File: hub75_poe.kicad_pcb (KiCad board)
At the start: 4 copper layers, 70.5 x 48.3 mm, 98 parts, among them J1 0826-1X1T-JK-F, J2 Conn_02x08_Odd_Even, J3 Conn_02x04_Odd_Even, Q1 FDS2582, Q2 FDS8880, SW1 SW_SPST, T1 PA2369NL, T2 PE-68386NL, U1 KSZ8081MLX, U10 SN74LVC8T245, U11 SN74LVC8T245, U12 OSC_100M, U2 ICE40HX8K-BG121, U3 LTC4269-1, U4 TPS74633, U5 TPS74612, U6 W25Q32JVSS, U7 S27KL0641, U8 OSC_25M, U9 TPS74618

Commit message: Routing changes, pullups, etc
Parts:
- added J4: Conn_01x04, Connector_Molex:Molex_CLIK-Mate_502382-0970_1x09-1MP_P1.25mm_Vertical, B.Cu at (180.7, 69.2)
- added J5: 7466003R, hub75_poe:7466003R, F.Cu at (180.1, 95.4)
- added R25: 10k, Resistor_SMD:R_0402_1005Metric, F.Cu at (183.1, 60.8)
- added R26: 10k, Resistor_SMD:R_0402_1005Metric, B.Cu at (170.3, 68.1)
- added R27: 10k, Resistor_SMD:R_0402_1005Metric, B.Cu at (165.5, 66.3)
- J3: value Conn_02x04_Odd_Even -> 7466003R; footprint Connector_PinHeader_2.54mm:PinHeader_2x04_P2.54mm_Vertical -> hub75_poe:7466003R
- L1: footprint Inductor_SMD:L_Bourns-SRN4018 -> Inductor_SMD:L_Bourns_SRN6045TA
- R15, R16, R17, R18, R19: value R -> 10k
- U12: value OSC_100M -> ASEMB-100.000MHZ-LY-T
- U8: value OSC_25M -> ASEMB-25.000MHZ-LC-T
- moved S1 17.3 mm to (181.4, 78.1), turned to 90 degrees
- moved J3 10.3 mm to (170.9, 95.2)
- moved C20 7.27 mm to (175.5, 90.4)
- moved C21 6.27 mm to (163.3, 59.7)
- moved C13 5.64 mm to (159.8, 94.7), turned to 180 degrees
- moved L1 3.89 mm to (156.6, 85.7)
- moved JP1 3.37 mm to (174.0, 87.0), turned to -90 degrees
- moved C22 1.83 mm to (164.5, 56.9), turned to 0 degrees
- moved C17 1.40 mm to (164.0, 66.3)
- moved C32 1.11 mm to (165.5, 62.4), turned to 90 degrees
- moved C16 0.76 mm to (170.8, 66.7)
- moved C29 0.71 mm to (168.7, 62.4), turned to 90 degrees
- moved C31 0.44 mm to (168.7, 68.0), turned to -90 degrees
- moved C33 0.38 mm to (166.5, 68.1), turned to -90 degrees
- moved R18 0.26 mm to (166.4, 72.3)
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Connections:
- net /CONFIG/CRESET renamed /CONFIG/~CRESET
- C16 pad 1: +1V2 -> Net-(C16-Pad1)
- C17 pad 1: +1V2 -> Net-(C17-Pad1)
- R16 pad 1: VCC -> GND
- R17 pad 1: VCC -> GND
- U2 pad B11: /MEMORY/~CS1 -> /MEMORY/~RESET1
- U2 pad C6: +1V2 -> Net-(C17-Pad1)
- U2 pad D10: /MEMORY/~RESET1 -> /MEMORY/~CS1
- U2 pad J6: +1V2 -> Net-(C16-Pad1)
- U2 pad K3: Net-(U2-PadK3) -> /CONFIG/DBG_AUX_A
- U2 pad K4: Net-(U2-PadK4) -> /CONFIG/DBG_AUX_B
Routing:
- net Net-(J4-Pad8): track 4.50 -> 19.5 mm, vias 0 -> 1
- net Net-(J4-Pad5): track 13.3 -> 26.7 mm
- net /CONFIG/DBG_AUX_A: track 0.00 -> 9.65 mm, vias 0 -> 1
- net Net-(J4-Pad7): track 11.2 -> 20.8 mm
- net /CONFIG/DBG_AUX_B: track 0.00 -> 9.47 mm, vias 0 -> 1
- net +1V8: track 60.3 -> 51.3 mm
- net Net-(J4-Pad6): track 11.7 -> 19.5 mm, vias 0 -> 1
- net VBUS: track 10.8 -> 5.28 mm
- net /CONFIG/~CRESET: track 3.08 -> 7.71 mm, vias 0 -> 1
- net VCC: track 122.5 -> 126.3 mm, vias 13 -> 15
- net +1V2: track 45.9 -> 42.3 mm, vias 7 -> 5
- net GND: track 63.7 -> 66.1 mm, vias 72 -> 77
- net /MEMORY/~CS1: track 8.51 -> 10.8 mm
- net Net-(C16-Pad1): track 0.00 -> 2.20 mm, vias 0 -> 1
- net /MEMORY/~RESET1: track 12.3 -> 10.2 mm
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
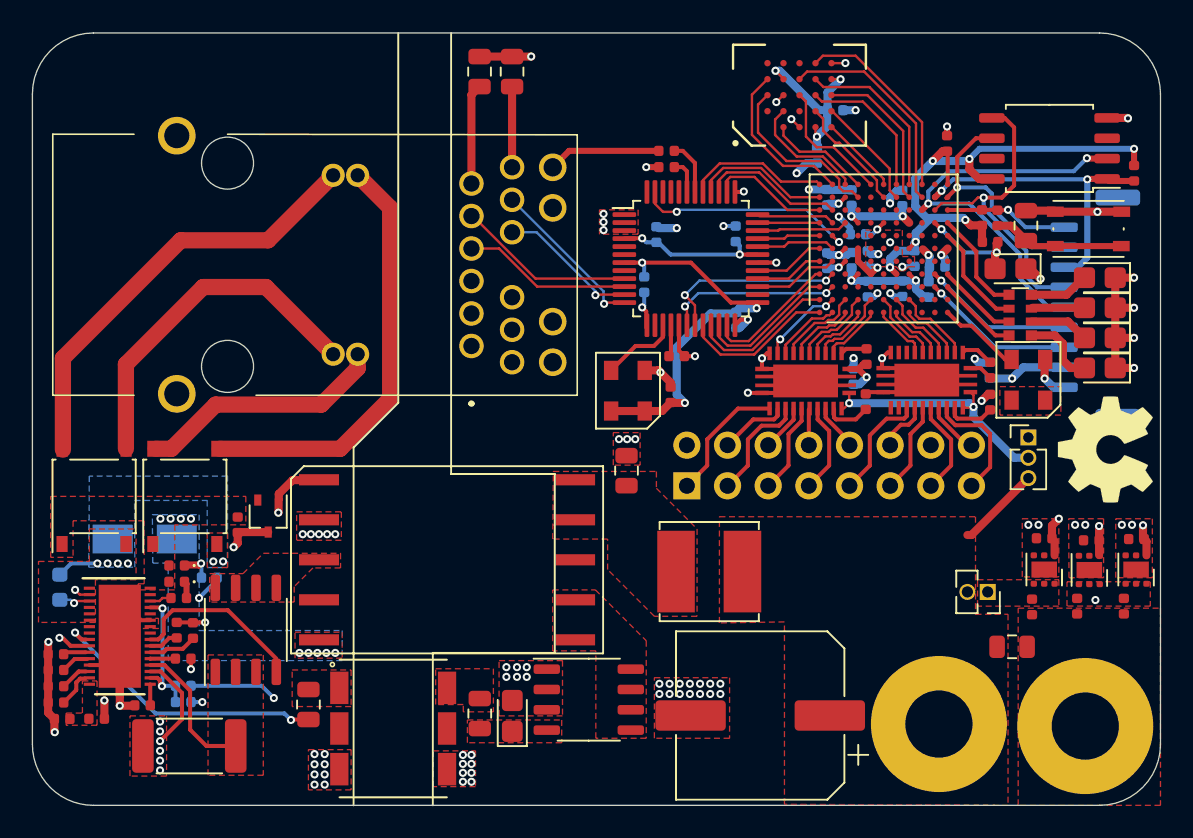
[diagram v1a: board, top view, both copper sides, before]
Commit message: Routing cleanup, fix primary transformer
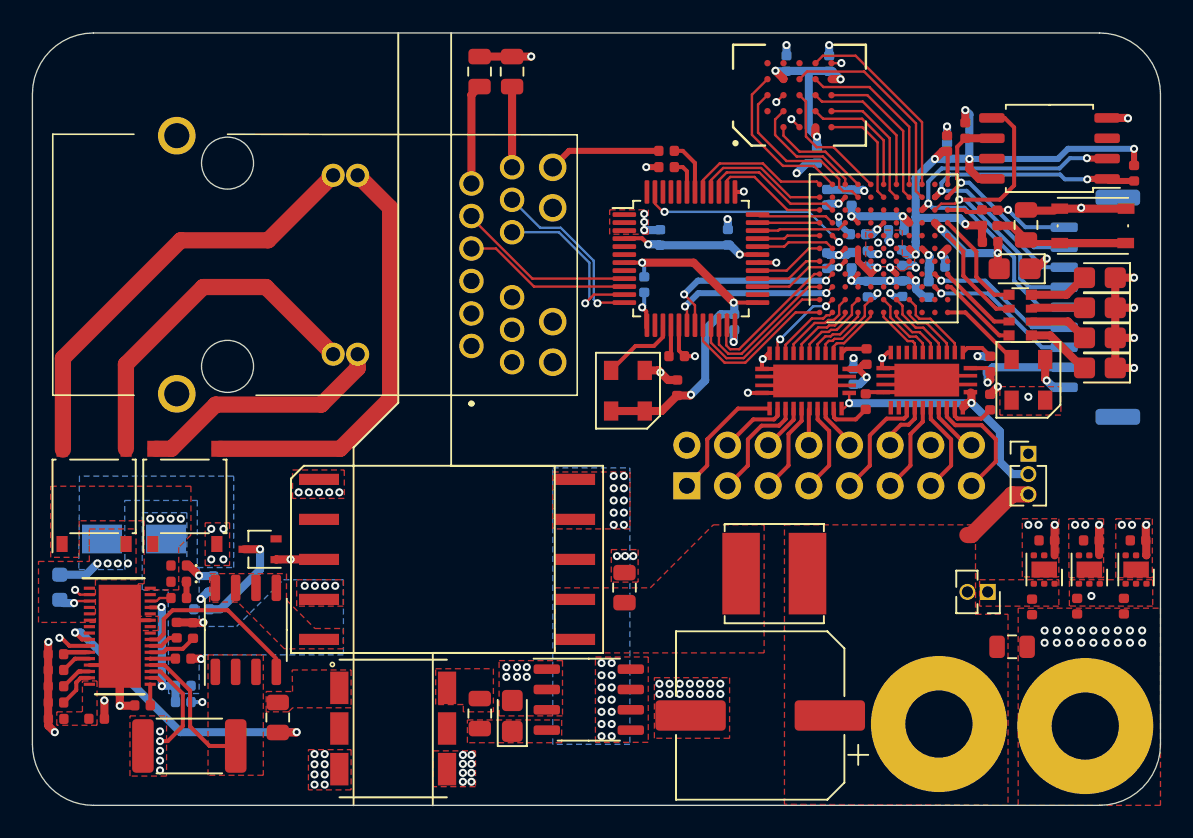
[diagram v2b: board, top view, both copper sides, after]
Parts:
- added C39: 10uf, Capacitor_SMD:C_0402_1005Metric, B.Cu at (161.4, 54.0)
- added C40: C, Capacitor_SMD:C_0402_1005Metric, B.Cu at (171.4, 59.4)
- added R28: 10k, Resistor_SMD:R_0402_1005Metric, F.Cu at (172.6, 58.2)
- C13: value 470uf -> 470uf+
- L1: value L -> SRN6045TA-2R2Y
- R11, S1: moved to B.Cu
- SW1: value SW_SPST -> 434133025816
- moved S1 27.6 mm to (158.2, 93.2), turned to 180 degrees
- moved C12 7.31 mm to (151.3, 86.7)
- moved R11 5.73 mm to (124.9, 88.1), turned to 0 degrees
- moved L1 4.07 mm to (160.7, 85.9)
- moved C22 2.95 mm to (164.1, 54.0), turned to 90 degrees
- moved D4 2.14 mm to (128.5, 84.3), turned to 180 degrees
- moved C10 2.08 mm to (129.6, 94.8)
- moved C29 2.04 mm to (168.3, 64.4), turned to 180 degrees
- moved JP2 1.02 mm to (176.5, 78.4)
- moved C5 0.79 mm to (168.6, 66.1)
- moved D3 0.67 mm to (120.7, 83.7)
- moved C35 0.60 mm to (154.6, 74.2)
- moved C36 0.53 mm to (157.8, 64.8)
- moved R22 0.46 mm to (125.6, 86.5), turned to 90 degrees
- moved C38 0.40 mm to (174.0, 72.8)
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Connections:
- J1 pad 21: (no net) -> GNDPWR
- J1 pad 22: (no net) -> GNDPWR
- T1 pad 1: Net-(D4-Pad1) -> Net-(Q1-Pad5)
- T1 pad 2: GNDPWR -> /POE/POE_P
- T1 pad 3: Net-(Q1-Pad5) -> Net-(D4-Pad1)
- T1 pad 5: /POE/POE_P -> GNDPWR
- U2 pad F10: /MEMORY/DQ1 -> /MEMORY/DQ7
- U2 pad F11: /MEMORY/DQ7 -> /MEMORY/DQ1
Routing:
- net /POE/POE_P: track 8.98 -> 0.00 mm, vias 10 -> 8
- net VCC: track 126.3 -> 132.1 mm, vias 15 -> 17
- net Net-(D4-Pad3): track 20.4 -> 25.2 mm
- net Net-(C18-Pad2): track 8.27 -> 12.6 mm
- net Net-(J4-Pad7): track 20.8 -> 24.4 mm
- net Net-(D4-Pad1): track 23.5 -> 20.3 mm
- net Net-(J4-Pad8): track 19.5 -> 17.0 mm
- net /RJ45/TXN: track 8.81 -> 10.9 mm
- net /MEMORY/DQ7: track 4.94 -> 6.88 mm
- net Net-(R5-Pad2): track 1.27 -> 2.93 mm
- net /HUB75/VSHIFT: track 15.8 -> 17.2 mm
- net /MEMORY/DQ6: track 7.08 -> 8.20 mm
- net Net-(D12-Pad1): track 3.24 -> 2.16 mm
- net Net-(J4-Pad6): track 19.5 -> 20.5 mm
- net Net-(C10-Pad1): track 17.7 -> 18.7 mm
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- added copper zone on B.Cu, net Net-(Q2-Pad5)
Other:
- board text added: "CERN OHL-W V2"
- board text added: "DO NOT LICK THIS SCIENCE (60V DC)"
- board text added: "UNNAMED POE BOARD R0.5 UNTESTED"
- board text removed: "DO NOT LICK THIS SCIENCE (~60V DC)"
- board text removed: "UNNAMED POE BOARD R0 UNTESTED"

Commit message: Change PoE controller to NCP1081
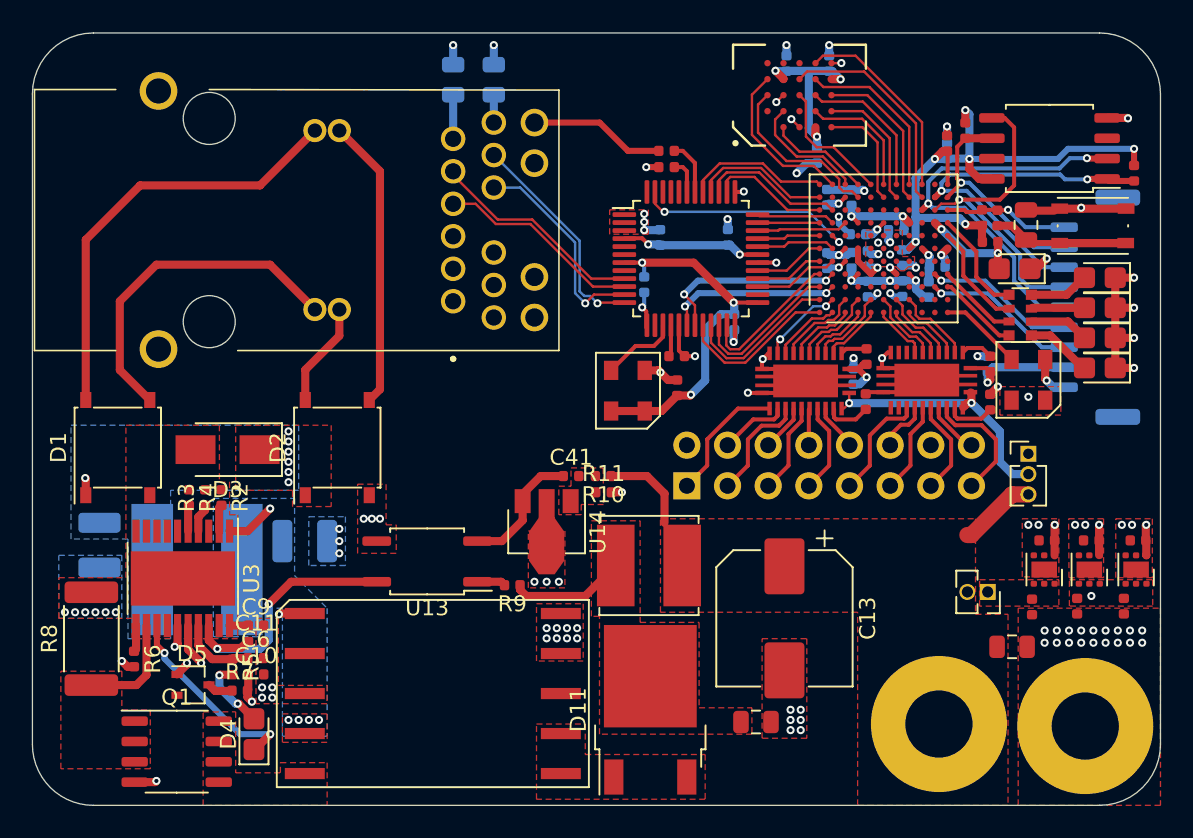
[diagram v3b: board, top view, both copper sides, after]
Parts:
- removed D12: LED, Diode_SMD:D_0402_1005Metric
- removed Q2: FDS8880, Package_SO:SOP-8_3.9x4.9mm_P1.27mm
- removed R12: 33m, Resistor_SMD:R_2512_6332Metric
- removed R21: 3.3k, Resistor_SMD:R_0402_1005Metric
- removed R22: 3k, Resistor_SMD:R_0402_1005Metric
- removed T2: PE-68386NL, hub75_poe:PE-68386NL
- added C41: C, Capacitor_SMD:C_0402_1005Metric, F.Cu at (148.0, 79.8)
- added L2: L, Inductor_SMD:L_Bourns-SRN8040_8x8.15mm, B.Cu at (124.6, 85.6)
- added U13: VO615A, Package_SO:SO-4_4.4x3.9mm_P2.54mm, F.Cu at (139.0, 85.1)
- added U14: TL431PK, Package_TO_SOT_SMD:SOT-89-3, F.Cu at (146.4, 82.8)
- C1, C2: moved to B.Cu
- C10: value 1uf -> C; footprint Capacitor_SMD:C_0805_2012Metric -> Capacitor_SMD:C_0402_1005Metric
- C11: value 2.2nf -> C; footprint Capacitor_SMD:C_0805_2012Metric -> Capacitor_SMD:C_0402_1005Metric
- C13: footprint Capacitor_SMD:CP_Elec_10x12.6 -> Capacitor_SMD:CP_Elec_8x10
- C6: value 10uf -> C
- C7: value 33pf -> C; footprint Capacitor_SMD:C_0402_1005Metric -> Capacitor_SMD:C_1210_3225Metric; moved to B.Cu
- C8: value 0.1uf -> C; footprint Capacitor_SMD:C_0402_1005Metric -> Capacitor_SMD:C_1210_3225Metric; moved to B.Cu
- C9: value 10nf -> C
- D1, D2: value ABS2 -> MBL104S; footprint Diode_SMD:Diode_Bridge_Diotec_ABS -> Diode_SMD:Diode_Bridge_Vishay_MBLS
- D11: value LED -> RFN5BGE3STL; footprint Diode_SMD:D_0402_1005Metric -> Package_TO_SOT_SMD:TO-252-2
- D3: moved to F.Cu
- D4: value BAS16W -> LED; footprint Package_TO_SOT_SMD:SOT-323_SC-70 -> Diode_SMD:D_0805_2012Metric_Castellated
- D5: value D_Schottky -> BAS16W; footprint Diode_SMD:D_0805_2012Metric_Castellated -> Package_TO_SOT_SMD:SOT-323_SC-70
- J4: value Conn_01x04 -> 502382-0970
- R10: value 3k -> R
- R11: value 39k -> R; moved to F.Cu
- R2: value 383k -> R; moved to F.Cu
- R3: value 14k -> R; moved to F.Cu
- R4: value 30.9 -> R; footprint Resistor_SMD:R_0603_1608Metric -> Resistor_SMD:R_0402_1005Metric; moved to F.Cu
- R5: value 100k -> R
- R6: value 38.3k -> R
- R7: value 12k -> R
- R8: value 1.21k -> R; footprint Resistor_SMD:R_0402_1005Metric -> Resistor_SMD:R_2512_6332Metric
- R9: value 27.4k -> R
- U3: value LTC4269-1 -> NCP1081; footprint Package_DFN_QFN:DFN-32-1EP_4x7mm_P0.4mm_EP2.64x6.44mm -> Package_SO:HTSSOP-20-1EP_4.4x6.5mm_P0.65mm_EP3.4x6.5mm
- moved R10 37.4 mm to (150.0, 79.8)
- moved D11 30.5 mm to (152.9, 94.4), turned to 90 degrees
- moved R9 27.3 mm to (144.3, 86.6)
- moved R11 26.2 mm to (150.0, 80.8)
- moved D5 20.0 mm to (124.3, 92.8), turned to 0 degrees
- moved C11 14.7 mm to (128.3, 90.1), turned to 0 degrees
- moved R3 12.9 mm to (125.1, 81.1), turned to 90 degrees
- moved C6 12.6 mm to (128.2, 91.1)
- moved R2 12.0 mm to (126.1, 81.1), turned to -90 degrees
- moved C12 11.7 mm to (159.5, 95.1), turned to 0 degrees
- moved D4 11.6 mm to (128.1, 95.9), turned to 90 degrees
- moved R5 11.1 mm to (126.8, 91.7), turned to -90 degrees
- moved C8 10.6 mm to (131.3, 83.8), turned to 0 degrees
- moved C7 10.2 mm to (118.5, 84.1), turned to -90 degrees
- moved D2 10.0 mm to (133.3, 78.0)
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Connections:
- C10 pad 2: Net-(C10-Pad2) -> GNDPWR
- C11 pad 2: Net-(C11-Pad2) -> GNDPWR
- C6 pad 1: GNDPWR -> Net-(C6-Pad1)
- C6 pad 2: Net-(C6-Pad2) -> GNDPWR
- C7 pad 1: GNDPWR -> /POE/POE_P
- C7 pad 2: Net-(C7-Pad2) -> GNDPWR
- C8 pad 1: GNDPWR -> Net-(C8-Pad1)
- C8 pad 2: Net-(C8-Pad2) -> GNDPWR
- D1 pad 2: /POE/POE_N -> GNDPWR
- D11 pad 2: /POE/POE_P -> Net-(C12-Pad1)
- D2 pad 2: /POE/POE_N -> GNDPWR
- D3 pad 2: /POE/POE_N -> GNDPWR
- D5 pad 1: Net-(C11-Pad2) -> Net-(D5-Pad1)
- D5 pad 2: GND -> Net-(D5-Pad2)
- R10 pad 1: Net-(R10-Pad1) -> VBUS
- R10 pad 2: GNDPWR -> Net-(C41-Pad2)
- R11 pad 1: /POE/POE_P -> Net-(C41-Pad2)
- R11 pad 2: Net-(D4-Pad3) -> GND
- R2 pad 1: /POE/POE_P -> GNDPWR
- R3 pad 1: Net-(R2-Pad2) -> Net-(R3-Pad1)
- R4 pad 1: Net-(R4-Pad1) -> GNDPWR
- R4 pad 2: /POE/POE_N -> Net-(R4-Pad2)
- R5 pad 1: GNDPWR -> Net-(C6-Pad1)
- R5 pad 2: Net-(R5-Pad2) -> Net-(D4-Pad2)
- R6 pad 1: GNDPWR -> Net-(R6-Pad1)
- R6 pad 2: Net-(R6-Pad2) -> GNDPWR
- R7 pad 1: GNDPWR -> Net-(D5-Pad3)
- R7 pad 2: Net-(R7-Pad2) -> Net-(C10-Pad1)
- R8 pad 1: GNDPWR -> Net-(Q1-Pad1)
- R8 pad 2: Net-(R8-Pad2) -> GNDPWR
- R9 pad 1: Net-(D4-Pad1) -> Net-(C12-Pad1)
- R9 pad 2: Net-(R10-Pad1) -> Net-(R9-Pad2)
- T1 pad 10: Net-(C12-Pad1) -> Net-(D11-Pad1)
- T1 pad 2: /POE/POE_P -> Net-(C8-Pad1)
- T1 pad 3: Net-(D4-Pad1) -> GNDPWR
- T1 pad 5: GNDPWR -> Net-(D5-Pad1)
- T1 pad 6: Net-(Q2-Pad5) -> GND
- T1 pad 7: Net-(Q2-Pad5) -> GND
- T1 pad 9: Net-(C12-Pad1) -> Net-(D11-Pad1)
- U3 pad 1: /POE/POE_N -> Net-(C8-Pad1)
- U3 pad 10: Net-(D4-Pad3) -> GNDPWR
- U3 pad 11: Net-(R5-Pad2) -> Net-(R6-Pad1)
- U3 pad 12: Net-(R6-Pad2) -> Net-(Q1-Pad1)
- U3 pad 13: GNDPWR -> Net-(D4-Pad1)
- U3 pad 14: Net-(C6-Pad2) -> GNDPWR
- U3 pad 15: Net-(C7-Pad2) -> Net-(Q1-Pad4)
- U3 pad 16: Net-(R10-Pad1) -> Net-(C10-Pad1)
- U3 pad 17: Net-(C9-Pad1) -> Net-(C6-Pad1)
- U3 pad 18: Net-(R2-Pad2) -> Net-(C11-Pad1)
- U3 pad 2: ~T2P -> Net-(R2-Pad2)
- U3 pad 20: Net-(Q1-Pad1) -> Net-(C9-Pad1)
- U3 pad 21: Net-(C8-Pad2) -> GNDPWR
- U3 pad 3: Net-(R4-Pad1) -> GNDPWR
- U3 pad 4: Net-(U3-Pad4) -> Net-(R3-Pad1)
- U3 pad 5: /POE/POE_N -> Net-(R4-Pad2)
- U3 pad 6: /POE/POE_N -> GNDPWR
- U3 pad 7: Net-(U3-Pad7) -> GNDPWR
- U3 pad 8: Net-(U3-Pad8) -> GNDPWR
- U3 pad 9: Net-(C10-Pad1) -> GNDPWR
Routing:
- net Net-(D4-Pad3): track 25.2 -> 0.00 mm, vias 2 -> 0
- net GNDPWR: track 25.8 -> 0.91 mm, vias 24 -> 17
- net Net-(C11-Pad1): track 0.00 -> 16.8 mm, vias 0 -> 2
- net ~T2P: track 10.1 -> 0.00 mm, vias 2 -> 0
- net Net-(D5-Pad1): track 0.00 -> 9.91 mm, vias 0 -> 2
- net Net-(C10-Pad1): track 18.7 -> 9.02 mm
- net /DATA_A: track 15.6 -> 6.54 mm
- net /DATA_B: track 26.7 -> 18.2 mm
- net Net-(D4-Pad1): track 20.3 -> 12.2 mm
- net Net-(C41-Pad1): track 0.00 -> 8.00 mm
- net Net-(C12-Pad1): track 0.00 -> 7.21 mm
- net Net-(R2-Pad2): track 8.61 -> 1.67 mm, vias 2 -> 0
- net VBUS: track 4.86 -> 10.5 mm
- net Net-(C6-Pad1): track 0.00 -> 4.71 mm
- net Net-(D4-Pad2): track 0.00 -> 4.56 mm, vias 0 -> 2
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- added copper zone on B.Cu, net GNDPWR
- added copper zone on F.Cu, net Net-(C41-Pad2)
- added copper zone on B.Cu, net Net-(C8-Pad1)
- added copper zone on F.Cu, net Net-(C8-Pad1)
- added copper zone on F.Cu, net Net-(D11-Pad1)
- removed copper zone on B.Cu, net /POE/POE_N
- removed copper zone on F.Cu, net /POE/POE_N
- removed copper zone on F.Cu, net Net-(C10-Pad2)
- removed copper zone on F.Cu, net Net-(C11-Pad1)
- removed copper zone on F.Cu, net Net-(C11-Pad2)
- removed copper zone on B.Cu, net Net-(Q2-Pad5)
- removed copper zone on F.Cu, net Net-(Q2-Pad5)
- removed copper zone on F.Cu, net Net-(R10-Pad1)
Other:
- net class HVDC: via_dia 0.4572 -> 0.508

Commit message: Update routing and icons/text
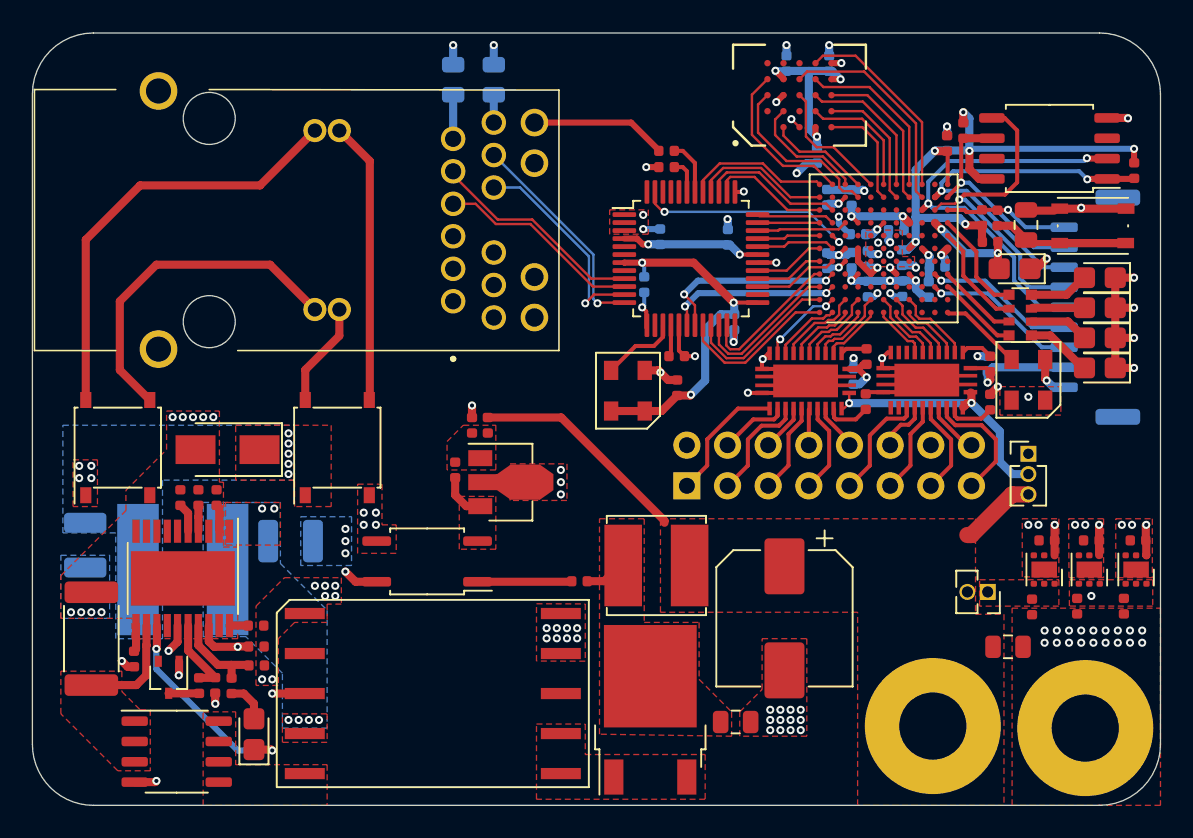
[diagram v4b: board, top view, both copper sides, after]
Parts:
- moved R11 9.23 mm to (141.8, 76.6), turned to 90 degrees
- moved R10 7.88 mm to (142.8, 76.6), turned to -90 degrees
- moved C41 7.25 mm to (140.7, 79.4), turned to 90 degrees
- moved R9 4.21 mm to (148.5, 86.3)
- moved U14 3.77 mm to (143.8, 80.1), turned to 0 degrees
- moved C10 2.64 mm to (125.7, 92.8), turned to -90 degrees
- moved R7 2.56 mm to (124.7, 92.8), turned to 90 degrees
- moved D5 1.59 mm to (122.8, 92.3), turned to -90 degrees
- moved C12 1.27 mm to (158.2, 95.1)
- moved R5 1.18 mm to (126.7, 92.9)
- moved C8 0.89 mm to (130.4, 83.8)
- moved L2 0.89 mm to (123.7, 85.6)
- moved C7 0.89 mm to (117.6, 84.1)
- moved R4 0.53 mm to (123.5, 81.1)
- moved C40 0.50 mm to (171.4, 58.9)
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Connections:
- T1 pad 3: GNDPWR -> Net-(D5-Pad1)
- T1 pad 5: Net-(D5-Pad1) -> GNDPWR
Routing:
- net VBUS: track 10.5 -> 18.7 mm
- net Net-(C12-Pad1): track 7.21 -> 2.34 mm
- net Net-(C41-Pad1): track 8.00 -> 3.38 mm
- net Net-(R9-Pad2): track 1.77 -> 5.90 mm
- net Net-(C10-Pad1): track 9.02 -> 4.96 mm, vias 2 -> 0
- net Net-(C8-Pad1): track 3.13 -> 0.00 mm, vias 5 -> 6
- net Net-(C11-Pad1): track 16.8 -> 14.5 mm
- net Net-(J4-Pad8): track 17.0 -> 14.9 mm
- net Net-(D4-Pad2): track 4.56 -> 2.60 mm, vias 2 -> 0
- net /POE/POE_P: track 1.08 -> 0.00 mm, vias 7 -> 9
- net Net-(C6-Pad1): track 4.71 -> 5.79 mm
- net Net-(D4-Pad1): track 12.2 -> 13.2 mm
- net Net-(D5-Pad1): track 9.91 -> 9.23 mm
- net GNDPWR: track 0.91 -> 1.58 mm, vias 17 -> 25
- net /DATA_B: track 18.2 -> 17.6 mm
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- added copper zone on F.Cu, net Net-(C41-Pad1)
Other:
- board text added: "PROJECT LIGHTNING PACKET R0.75 UNTESTED"
- board text removed: "UNNAMED POE BOARD R0.5 UNTESTED"
